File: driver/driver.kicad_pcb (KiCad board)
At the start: 2 copper layers, 100 x 100 mm, 104 parts, among them J1 OUT_A, J2 OUT_B, J3 UART_DEBUG, J4 USB_B_Micro, J5 CH340E module, J6 1602 I2C LCD, J7 IN_VCC, J8 IN_GND, J9 SWD, Q1 TPHR6503PL, Q2 TPHR6503PL, Q3 TPHR6503PL, Q4 TPHR6503PL, SW1 SW_Push, SW2 SW_Push, U1 MT3608, U10 PC817, U2 AMS1117-5.0, U3 AMS1117-3.3, U4 TC4427, U5 TC4427, U6 STM32F103C8Tx, U7 INA226, U8 MCP9804_MSOP, U9 PC817, Y1 8MHz

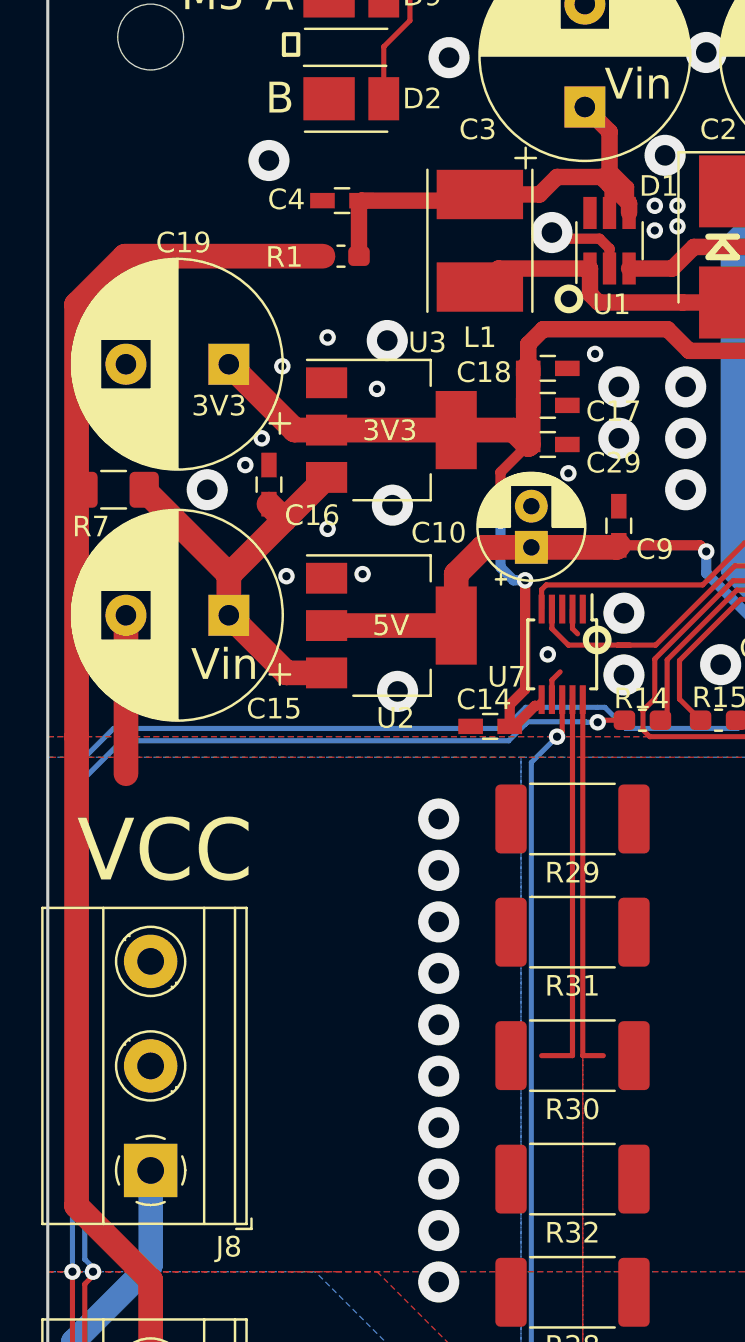
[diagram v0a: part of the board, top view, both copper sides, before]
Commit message: Fix R1 footprint
0603 -> 1206
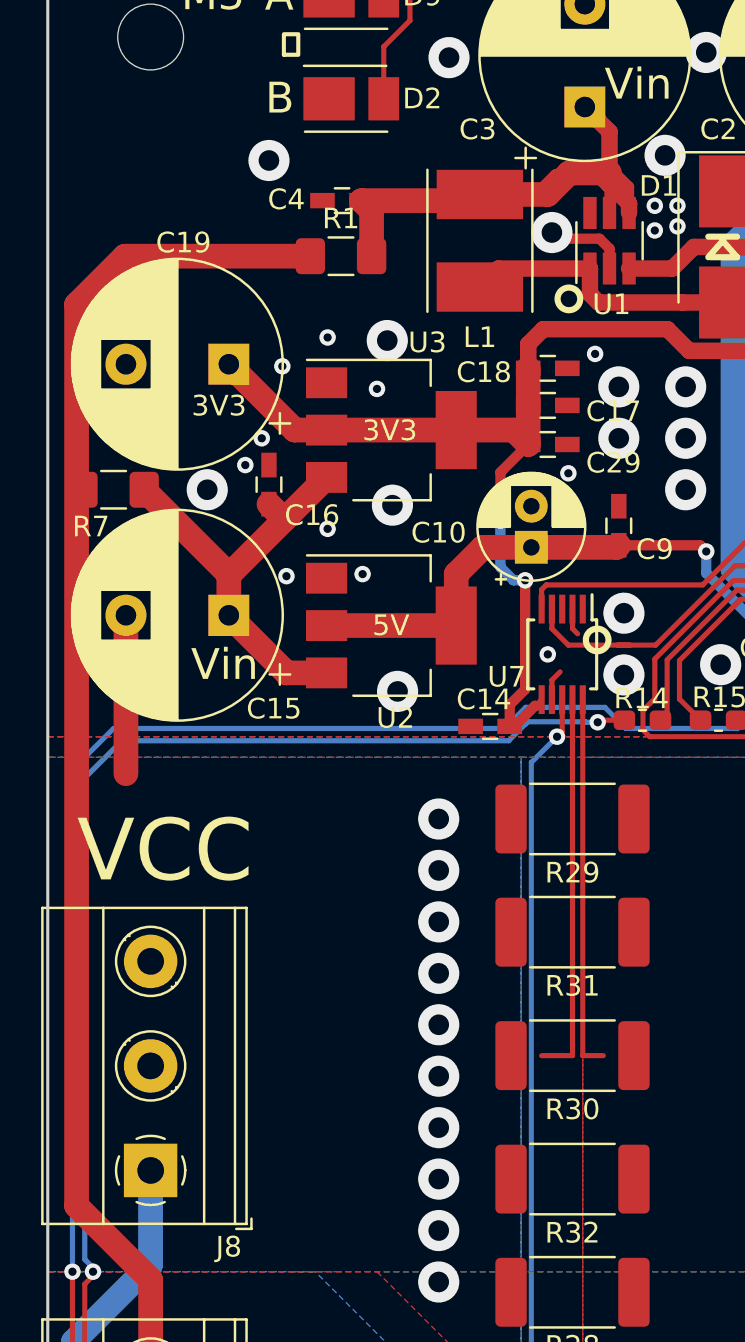
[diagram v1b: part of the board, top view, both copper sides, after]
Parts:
- R1: footprint Resistor_SMD:R_0603_1608Metric_Pad1.05x0.95mm_HandSolder -> Resistor_SMD:R_1206_3216Metric_Pad1.42x1.75mm_HandSolder
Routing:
- net Net-(C3-Pad1): track 28.9 -> 35.8 mm
- net /VIN: track 111.0 -> 110.4 mm
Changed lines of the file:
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@@
     (thickness 1.6)
     (drawings 127)
-    (tracks 1376)
+    (tracks 1379)
     (zones 0)
     (modules 104)
@@
   )
   (setup
-    (last_trace_width 0.25)
+    (last_trace_width 1.2)
     (user_trace_width 0.15)
     (user_trace_width 0.25)
@@
   )
   (module Resistor_SMD:R_0603_1608Metric_Pad1.05x0.95mm_HandSolder (layer F.Cu)
-    (at 84.25 70.65)
-    (descr "Resistor SMD 0603 (1608 Metric), square (rectangular) end terminal, IPC_7351 nominal with elongated pad for handsoldering. (Body size source: http://www.tortai-tech.com/upload/download/2011102023233369053.pdf), generated with kicad-footprint-generator")
-    (tags "resistor handsolder")
-    (attr smd)
-    (fp_text reference R1 (at -2.75 0.05) (layer F.SilkS)
-      (effects (font (size 1 1) (thickness 0.15)))
-    )
-    (fp_text value "10R .5W" (at 0 1.43) (layer F.Fab)
-      (effects (font (size 1 1) (thickness 0.15)))
-    )
-    (fp_text user %R (at 0 0) (layer F.Fab)
-      (effects (font (size 0.4 0.4) (thickness 0.06)))
-    )
-    (fp_line (start 1.65 0.73) (end -1.65 0.73) (layer F.CrtYd) (width 0.05))
-    (fp_line (start 1.65 -0.73) (end 1.65 0.73) (layer F.CrtYd) (width 0.05))
-    (fp_line (start -1.65 -0.73) (end 1.65 -0.73) (layer F.CrtYd) (width 0.05))
-    (fp_line (start -1.65 0.73) (end -1.65 -0.73) (layer F.CrtYd) (width 0.05))
-    (fp_line (start -0.171267 0.51) (end 0.171267 0.51) (layer F.SilkS) (width 0.12))
-    (fp_line (start -0.171267 -0.51) (end 0.171267 -0.51) (layer F.SilkS) (width 0.12))
-    (fp_line (start 0.8 0.4) (end -0.8 0.4) (layer F.Fab) (width 0.1))
-    (fp_line (start 0.8 -0.4) (end 0.8 0.4) (layer F.Fab) (width 0.1))
-    (fp_line (start -0.8 -0.4) (end 0.8 -0.4) (layer F.Fab) (width 0.1))
-    (fp_line (start -0.8 0.4) (end -0.8 -0.4) (layer F.Fab) (width 0.1))
-    (pad 2 smd roundrect (at 0.875 0) (size 1.05 0.95) (layers F.Cu F.Paste F.Mask) (roundrect_rratio 0.25)
-      (net 3 "Net-(C3-Pad1)"))
-    (pad 1 smd roundrect (at -0.875 0) (size 1.05 0.95) (layers F.Cu F.Paste F.Mask) (roundrect_rratio 0.25)
-      (net 70 /VIN))
-    (model ${KISYS3DMOD}/Resistor_SMD.3dshapes/R_0603_1608Metric.wrl
-      (at (xyz 0 0 0))
-      (scale (xyz 1 1 1))
-      (rotate (xyz 0 0 0))
-    )
-  )
-  (module Resistor_SMD:R_0603_1608Metric_Pad1.05x0.95mm_HandSolder (layer F.Cu)
     (at 107.7 69.1)
     (descr "Resistor SMD 0603 (1608 Metric), square (rectangular) end terminal, IPC_7351 nominal with elongated pad for handsoldering. (Body size source: http://www.tortai-tech.com/upload/download/2011102023233369053.pdf), generated with kicad-footprint-generator")
@@
     )
   )
+  (module Resistor_SMD:R_1206_3216Metric_Pad1.42x1.75mm_HandSolder (layer F.Cu)
+    (at 84.25 70.65)
+    (descr "Resistor SMD 1206 (3216 Metric), square (rectangular) end terminal, IPC_7351 nominal with elongated pad for handsoldering. (Body size source: http://www.tortai-tech.com/upload/download/2011102023233369053.pdf), generated with kicad-footprint-generator")
+    (tags "resistor handsolder")
+    (attr smd)
+    (fp_text reference R1 (at 0 -1.82) (layer F.SilkS)
+      (effects (font (size 1 1) (thickness 0.15)))
+    )
+    (fp_text value "10R .5W" (at 0 1.82) (layer F.Fab)
+      (effects (font (size 1 1) (thickness 0.15)))
+    )
+    (fp_line (start -1.6 0.8) (end -1.6 -0.8) (layer F.Fab) (width 0.1))
+    (fp_line (start -1.6 -0.8) (end 1.6 -0.8) (layer F.Fab) (width 0.1))
+    (fp_line (start 1.6 -0.8) (end 1.6 0.8) (layer F.Fab) (width 0.1))
+    (fp_line (start 1.6 0.8) (end -1.6 0.8) (layer F.Fab) (width 0.1))
+    (fp_line (start -0.602064 -0.91) (end 0.602064 -0.91) (layer F.SilkS) (width 0.12))
+    (fp_line (start -0.602064 0.91) (end 0.602064 0.91) (layer F.SilkS) (width 0.12))
+    (fp_line (start -2.45 1.12) (end -2.45 -1.12) (layer F.CrtYd) (width 0.05))
+    (fp_line (start -2.45 -1.12) (end 2.45 -1.12) (layer F.CrtYd) (width 0.05))
+    (fp_line (start 2.45 -1.12) (end 2.45 1.12) (layer F.CrtYd) (width 0.05))
+    (fp_line (start 2.45 1.12) (end -2.45 1.12) (layer F.CrtYd) (width 0.05))
+    (fp_text user %R (at 0 0) (layer F.Fab)
+      (effects (font (size 0.8 0.8) (thickness 0.12)))
+    )
+    (pad 1 smd roundrect (at -1.4875 0) (size 1.425 1.75) (layers F.Cu F.Paste F.Mask) (roundrect_rratio 0.175439)
+      (net 70 /VIN))
+    (pad 2 smd roundrect (at 1.4875 0) (size 1.425 1.75) (layers F.Cu F.Paste F.Mask) (roundrect_rratio 0.175439)
+      (net 3 "Net-(C3-Pad1)"))
+    (model ${KISYS3DMOD}/Resistor_SMD.3dshapes/R_1206_3216Metric.wrl
+      (at (xyz 0 0 0))
+      (scale (xyz 1 1 1))
+      (rotate (xyz 0 0 0))
+    )
+  )
   (gr_circle (center 96.7 89.3) (end 97.25 89.3) (layer F.SilkS) (width 0.3))
   (gr_text Vin (at 78.6 90.5) (layer F.SilkS)
@@
   (segment (start 97.3 67.2) (end 97.3 65.5) (width 0.5) (layer F.Cu) (net 3))
   (segment (start 96.1 63.4) (end 97.3 64.6) (width 0.8) (layer F.Cu) (net 3))
-  (segment (start 97.3 64.6) (end 97.3 67.2) (width 0.8) (layer F.Cu) (net 3))
   (segment (start 93.9 67.65) (end 91 67.65) (width 0.8) (layer F.Cu) (net 3))
   (segment (start 94.75 66.8) (end 93.9 67.65) (width 0.8) (layer F.Cu) (net 3))
@@
   (segment (start 98.25 68.095) (end 97.355 67.2) (width 0.8) (layer F.Cu) (net 3))
   (segment (start 98.25 68.55) (end 98.25 68.095) (width 0.8) (layer F.Cu) (net 3))
-  (segment (start 85.125 68.075) (end 85.25 67.95) (width 0.8) (layer F.Cu) (net 3))
-  (segment (start 85.125 70.65) (end 85.125 68.075) (width 0.8) (layer F.Cu) (net 3))
-  (segment (start 90.7 67.95) (end 91 67.65) (width 0.8) (layer F.Cu) (net 3))
-  (segment (start 85.25 67.95) (end 90.7 67.95) (width 0.8) (layer F.Cu) (net 3))
+  (segment (start 85.7375 68.4375) (end 85.25 67.95) (width 1.2) (layer F.Cu) (net 3))
+  (segment (start 85.7375 70.65) (end 85.7375 68.4375) (width 1.2) (layer F.Cu) (net 3))
+  (segment (start 90.7 67.95) (end 91 67.65) (width 1.2) (layer F.Cu) (net 3))
+  (segment (start 85.25 67.95) (end 90.7 67.95) (width 1.2) (layer F.Cu) (net 3))
+  (segment (start 94.3 67.65) (end 91 67.65) (width 1.2) (layer F.Cu) (net 3))
+  (segment (start 95.35 66.6) (end 94.3 67.65) (width 1.2) (layer F.Cu) (net 3))
+  (segment (start 97.3 66.6) (end 95.35 66.6) (width 1.2) (layer F.Cu) (net 3))
+  (segment (start 97.3 66.6) (end 97.3 67.2) (width 0.8) (layer F.Cu) (net 3))
+  (segment (start 97.3 64.6) (end 97.3 66.6) (width 0.8) (layer F.Cu) (net 3))
   (segment (start 116.350001 66.424999) (end 116.4 66.375) (width 0.5) (layer F.Cu) (net 4))
   (segment (start 114.325001 66.424999) (end 116.350001 66.424999) (width 0.5) (layer F.Cu) (net 4))
@@
   (via (at 130 139) (size 0.8) (drill 0.4) (layers F.Cu B.Cu) (net 70))
   (via (at 131 139) (size 0.8) (drill 0.4) (layers F.Cu B.Cu) (net 70))
-  (segment (start 73.75 70.65) (end 83.375 70.65) (width 1.2) (layer F.Cu) (net 70))
-  (segment (start 71.4 73) (end 73.75 70.65) (width 1.2) (layer F.Cu) (net 70))
-  (segment (start 71.4 94) (end 71.4 73) (width 1.2) (layer F.Cu) (net 70))
   (via (at 94.75 94) (size 0.8) (drill 0.4) (layers F.Cu B.Cu) (net 70))
   (segment (start 95 92.2) (end 95 93.75) (width 0.25) (layer F.Cu) (net 70))
@@
   (segment (start 94.75 94) (end 93.5 95.25) (width 0.25) (layer B.Cu) (net 70))
   (segment (start 93.5 95.25) (end 93.5 124.75) (width 0.25) (layer B.Cu) (net 70))
-  (segment (start 75 124.92) (end 75 120.4) (width 1.2) (layer F.Cu) (net 70))
-  (segment (start 75 120.4) (end 71.4 116.8) (width 1.2) (layer F.Cu) (net 70))
-  (segment (start 71.4 94) (end 71.4 116.8) (width 1.2) (layer F.Cu) (net 70))
   (segment (start 110.575 93.675) (end 110.575 92.3) (width 0.25) (layer F.Cu) (net 70))
   (segment (start 111 94.1) (end 110.575 93.675) (width 0.25) (layer F.Cu) (net 70))
@@
   (segment (start 116.2 96.5) (end 113.8 94.1) (width 0.25) (layer F.Cu) (net 70))
   (segment (start 118 96.5) (end 116.2 96.5) (width 0.25) (layer F.Cu) (net 70))
+  (segment (start 73.75 70.65) (end 82.7625 70.65) (width 1.2) (layer F.Cu) (net 70))
+  (segment (start 71.4 73) (end 73.75 70.65) (width 1.2) (layer F.Cu) (net 70))
+  (segment (start 71.4 116.8) (end 71.4 73) (width 1.2) (layer F.Cu) (net 70))
+  (segment (start 75 124.92) (end 75 120.4) (width 1.2) (layer F.Cu) (net 70))
+  (segment (start 75 120.4) (end 71.4 116.8) (width 1.2) (layer F.Cu) (net 70))
   (segment (start 96 92.2) (end 96 109.5) (width 0.25) (layer F.Cu) (net 71))
   (segment (start 96 109.5) (end 97 109.5) (width 0.25) (layer F.Cu) (net 71))

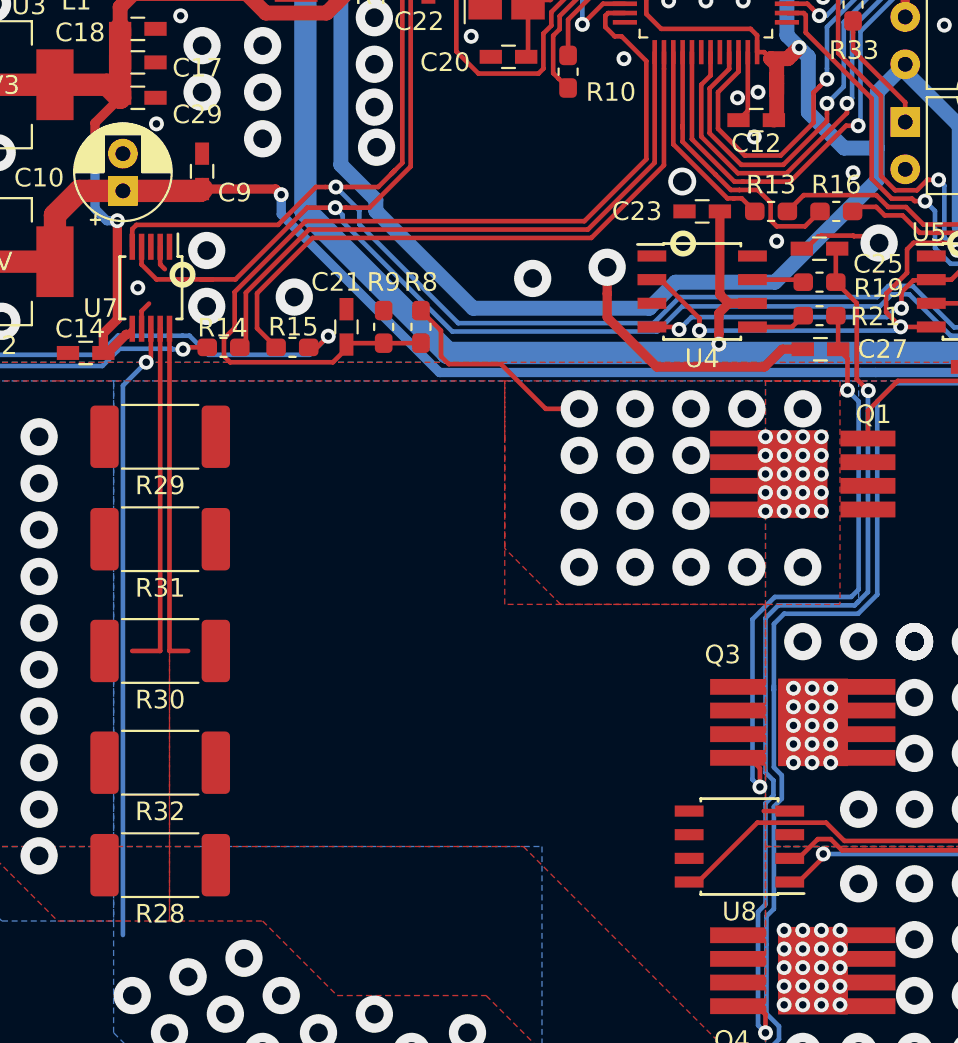
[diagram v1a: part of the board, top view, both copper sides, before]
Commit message: Modify temp sensor to MSOP fp, add fan conn
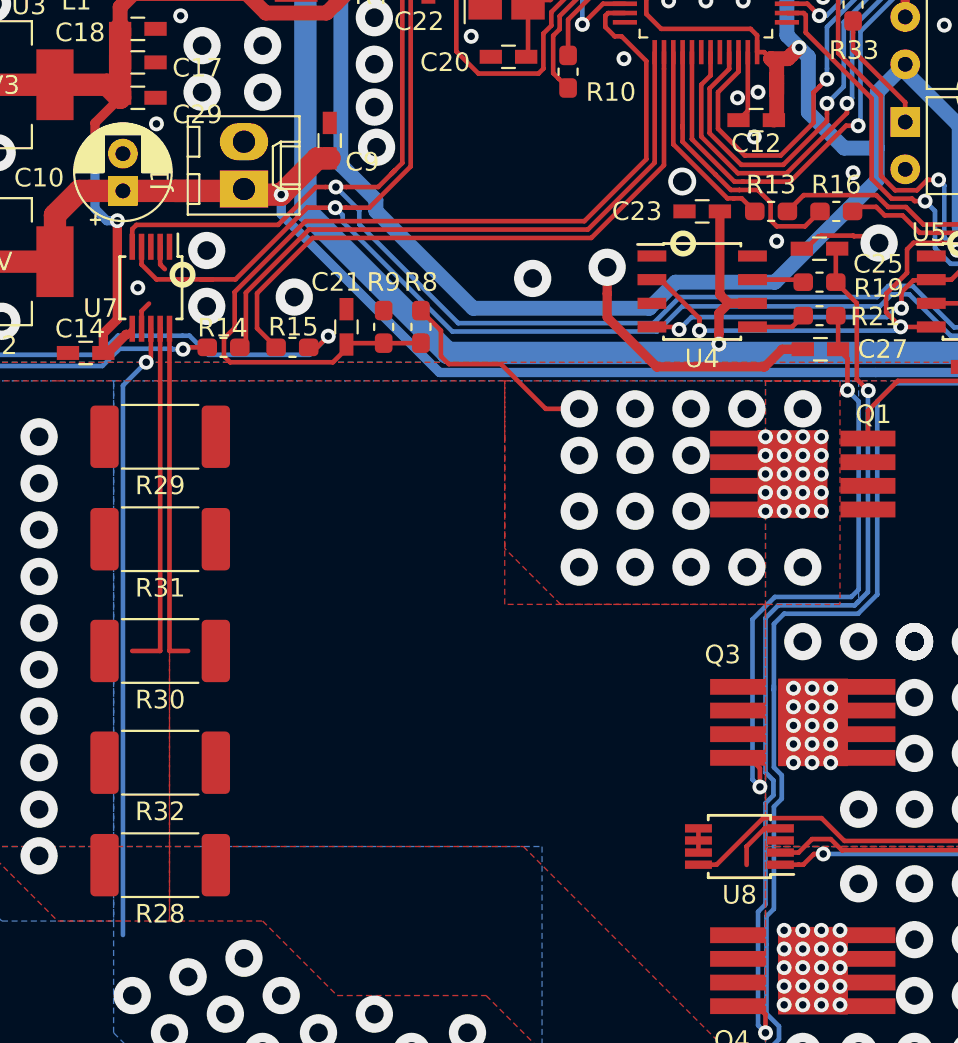
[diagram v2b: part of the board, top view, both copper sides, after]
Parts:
- added J10: FAN, Connectors_Molex:Molex_KK-6410-02_02x2.54mm_Straight, F.Cu at (100.0, 84.7)
- U8: footprint Package_SO:SOIC-8_3.9x4.9mm_P1.27mm -> Package_SO:MSOP-8_3x3mm_P0.65mm
- moved C9 7.05 mm to (104.6, 82.1)
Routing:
- net +5V: track 106.8 -> 116.0 mm
- net /GND_MEAS: track 19.7 -> 22.8 mm
- net +3V3: track 329.8 -> 329.1 mm
- net GND: vias 83 -> 82
